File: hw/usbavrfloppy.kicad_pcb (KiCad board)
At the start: 2 copper layers, 96.5 x 70.5 mm, 65 parts, among them CON1 CONN_02X03, J1 bothdrv, J2 floppy_conn, J3 floppy_power, J5 USB_B, J6 PWRIN, J7 USB_OTG, P1 CONN_01X03, P2 CONN_01X01, P3 CONN_01X01, P4 CONN_01X01, P5 CONN_01X01, Q1 BSS138, Q10 BSS138, Q2 BSS138, Q3 BSS138, Q4 BSS138, Q5 BSS138, Q6 BSS138, Q7 BSS138, Q8 BSS138, Q9 BSS138, SW1 ~mRESET, U1 ATMEGA88-A, U2 FT232RL, Y1 16MHz

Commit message: First Kicad 5 import
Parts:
- removed G***: LOGO, RetroBitLab:amigaLogo_BW_31x12mm
- removed OSHW: Symbol_OSHW-Logo_SilkScreen, Symbols:Symbol_OSHW-Logo_SilkScreen
- removed WB: LOGO, RetroBitLab:amigaWorkBench1-SIlkScreenBack
- added AmigaLogo: LOGO, RetroBitLab:amigaLogo_BW_31x12mm, B.Cu at (151.8, 105.4)
- added J4: FPC Floppy, RetroBitLab:HLW26R-6C7LF, B.Cu at (152.4, 125.7)
- added KicadLogo: KiCad-Logo2_5mm_SilkScreen, Symbol:KiCad-Logo2_5mm_SilkScreen, F.Cu at (158.8, 88.3)
- added WBLogo: LOGO, RetroBitLab:amigaWorkBench1, B.Cu at (184.2, 69.8)
- C1, C2, C3, C4, C6: footprint Capacitors_SMD:C_1206_HandSoldering -> Capacitor_SMD:C_1206_3216Metric_Pad1.33x1.80mm_HandSolder
- C5: footprint Capacitors_SMD:c_elec_5x5.7 -> Capacitor_Tantalum_SMD:CP_EIA-3216-18_Kemet-A_Pad1.58x1.35mm_HandSolder
- CON1: value CONN_02X03 -> Conn_02x03; footprint Pin_Headers:Pin_Header_Angled_2x03 -> Connector_PinHeader_2.54mm:PinHeader_2x03_P2.54mm_Horizontal
- D1, D2, D3: footprint LEDs:LED_1206 -> LED_SMD:LED_1206_3216Metric_Pad1.42x1.75mm_HandSolder
- J1: footprint Pin_Headers:Pin_Header_Straight_1x02 -> Connector_PinHeader_2.54mm:PinHeader_1x02_P2.54mm_Vertical
- J3: footprint Pin_Headers:Pin_Header_Straight_1x04 -> Connector_PinHeader_2.54mm:PinHeader_1x04_P2.54mm_Vertical
- J6: footprint Pin_Headers:Pin_Header_Angled_1x04 -> Connector_PinHeader_2.54mm:PinHeader_1x04_P2.54mm_Horizontal
- P1: footprint Pin_Headers:Pin_Header_Straight_1x03 -> Connector_PinHeader_2.54mm:PinHeader_1x03_P2.54mm_Vertical
- P2, P3, P4, P5: footprint Connect:1pin -> MountingHole:MountingHole_3mm
- Q1, Q10, Q2, Q3, Q4, Q5, Q6, Q7, Q8, Q9: footprint TO_SOT_Packages_SMD:SOT-23 -> Package_TO_SOT_SMD:SOT-23
- R1, R10, R11, R12, R13, R14, R15, R16, R17, R18, R19, R2, R20, R21, R22, R23, R24, R25, R26, R27, R3, R4, R5, R6, R7, R8, R9: footprint Resistors_SMD:R_1206_HandSoldering -> Resistor_SMD:R_1206_3216Metric_Pad1.30x1.75mm_HandSolder
- U1: value ATMEGA88-A -> ATmega88PA-AU; footprint Housings_QFP:TQFP-32_7x7mm_Pitch0.8mm -> Package_QFP:TQFP-32_7x7mm_P0.8mm
- U2: footprint Housings_SSOP:SSOP-28_5.3x10.2mm_Pitch0.65mm -> Package_SO:SSOP-28_5.3x10.2mm_P0.65mm
- Y1: footprint Crystals:Crystal_HC49-SD_SMD -> Crystal:Crystal_HC49-4H_Vertical
- moved P4 15.2 mm to (196.8, 62.2)
- moved J6 11.7 mm to (177.8, 68.6)
- moved C4 2.83 mm to (126.0, 88.9)
- moved Y1 2.54 mm to (147.3, 80.0)
- moved C5 1.27 mm to (128.3, 82.5), turned to 270 degrees
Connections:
- J2 pad 2: (no net) -> Net-(J2-Pad2)
- J2 pad 34: (no net) -> Net-(J2-Pad34)
- J2 pad 4: (no net) -> Net-(J2-Pad4)
- J2 pad 6: (no net) -> Net-(J2-Pad6)
- J7 pad 4: (no net) -> Net-(J7-Pad4)
- P2 pad 1: (no net) -> Net-(P2-Pad1)
- P3 pad 1: (no net) -> Net-(P3-Pad1)
- P4 pad 1: (no net) -> Net-(P4-Pad1)
- P5 pad 1: (no net) -> Net-(P5-Pad1)
- U1 pad 14: (no net) -> Net-(U1-Pad14)
- U1 pad 19: (no net) -> Net-(U1-Pad19)
- U1 pad 20: (no net) -> Net-(U1-Pad20)
- U1 pad 22: (no net) -> Net-(U1-Pad22)
- U1 pad 26: (no net) -> Net-(U1-Pad26)
- U1 pad 27: (no net) -> Net-(U1-Pad27)
- U1 pad 28: (no net) -> Net-(U1-Pad28)
- U2 pad 10: (no net) -> Net-(U2-Pad10)
- U2 pad 12: (no net) -> Net-(U2-Pad12)
- U2 pad 13: (no net) -> Net-(U2-Pad13)
- U2 pad 14: (no net) -> Net-(U2-Pad14)
- U2 pad 19: (no net) -> Net-(U2-Pad19)
- U2 pad 2: (no net) -> Net-(U2-Pad2)
- U2 pad 22: (no net) -> Net-(U2-Pad22)
- U2 pad 23: (no net) -> Net-(U2-Pad23)
- U2 pad 27: (no net) -> Net-(U2-Pad27)
- U2 pad 28: (no net) -> Net-(U2-Pad28)
- U2 pad 3: (no net) -> Net-(U2-Pad3)
- U2 pad 6: (no net) -> Net-(U2-Pad6)
- U2 pad 9: (no net) -> Net-(U2-Pad9)
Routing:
- net Vcc_FLOPPY: track 318.4 -> 361.1 mm, vias 2 -> 1
- net GND: track 316.1 -> 292.6 mm, vias 1 -> 0
- net /~WDATA: track 42.0 -> 60.2 mm
- net /~mMOTEN: track 51.3 -> 34.6 mm
- net /CTS: track 46.2 -> 29.7 mm, vias 0 -> 2
- net /~DIR: track 36.1 -> 51.2 mm, vias 1 -> 0
- net /~MOTEB: track 46.1 -> 59.8 mm, vias 1 -> 0
- net /~mRESET: track 64.1 -> 51.6 mm, vias 0 -> 2
- net /~STEP: track 39.9 -> 51.4 mm, vias 1 -> 0
- net /~SIDE1: track 51.9 -> 62.6 mm
- net /~RDATA: track 26.8 -> 37.2 mm, vias 1 -> 0
- net /~WGATE: track 30.4 -> 40.4 mm
- net /~WPROT: track 23.3 -> 33.1 mm, vias 1 -> 0
- net VCC_USB: track 30.0 -> 37.1 mm, vias 2 -> 1
- net +12V: track 40.3 -> 34.8 mm
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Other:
- board text added: "Original concept on GitHub: RobSmithDev/ArduinoFloppyDiskReader"
- board text added: "P1 (1-2) = External VCC P1 (2-3) = USB Powered (max 500mA)"
- board text added: "RBL003.6"
- board text added: "designed by R.G. 2018/2019/2021"
- board text added: "https://github.com/gianlucarenzi/waffle-usbamigafloppy"
- board text removed: "RBL003.5"
- board text removed: "RETROBIT LAB"
- board text removed: "designed by R.G. 2018/2019"

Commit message: Updated
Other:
- board text added: "pin 1"
- board text added: "pin 26"

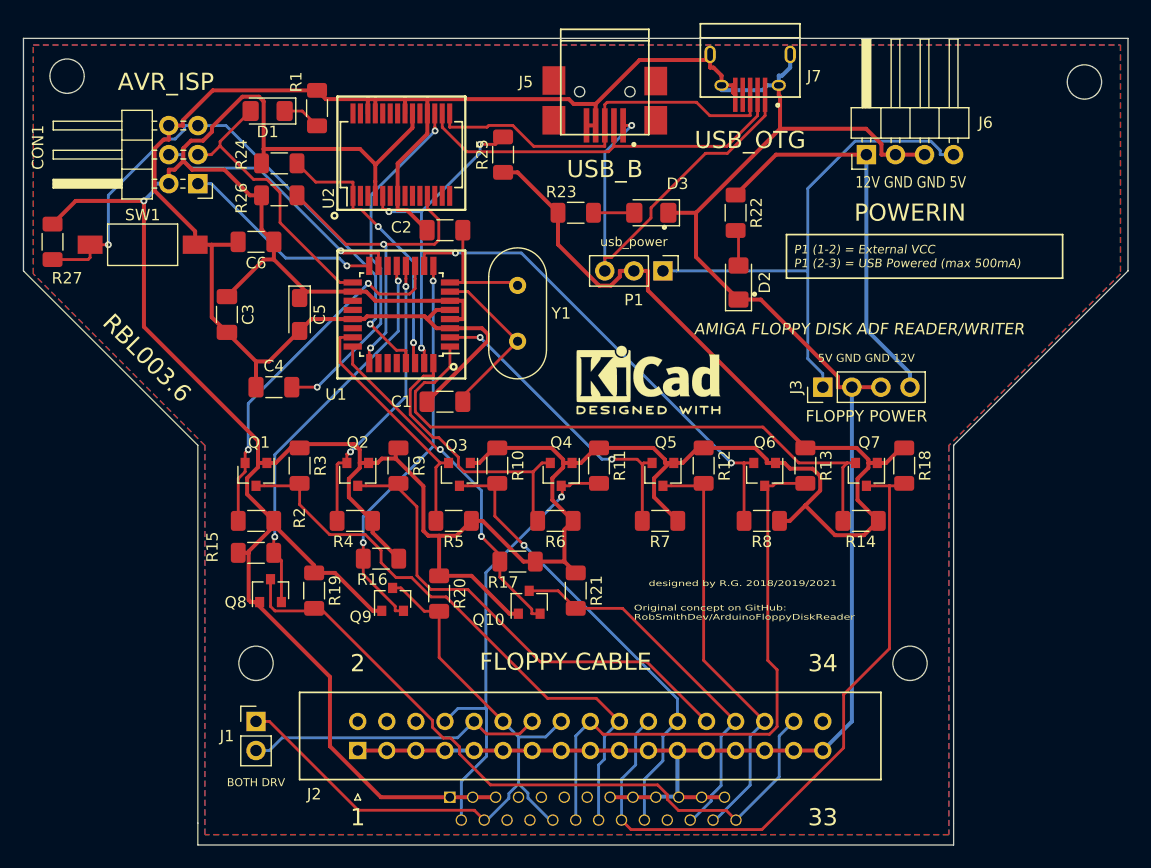
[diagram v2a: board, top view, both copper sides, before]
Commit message: Modified for final Kicad 5
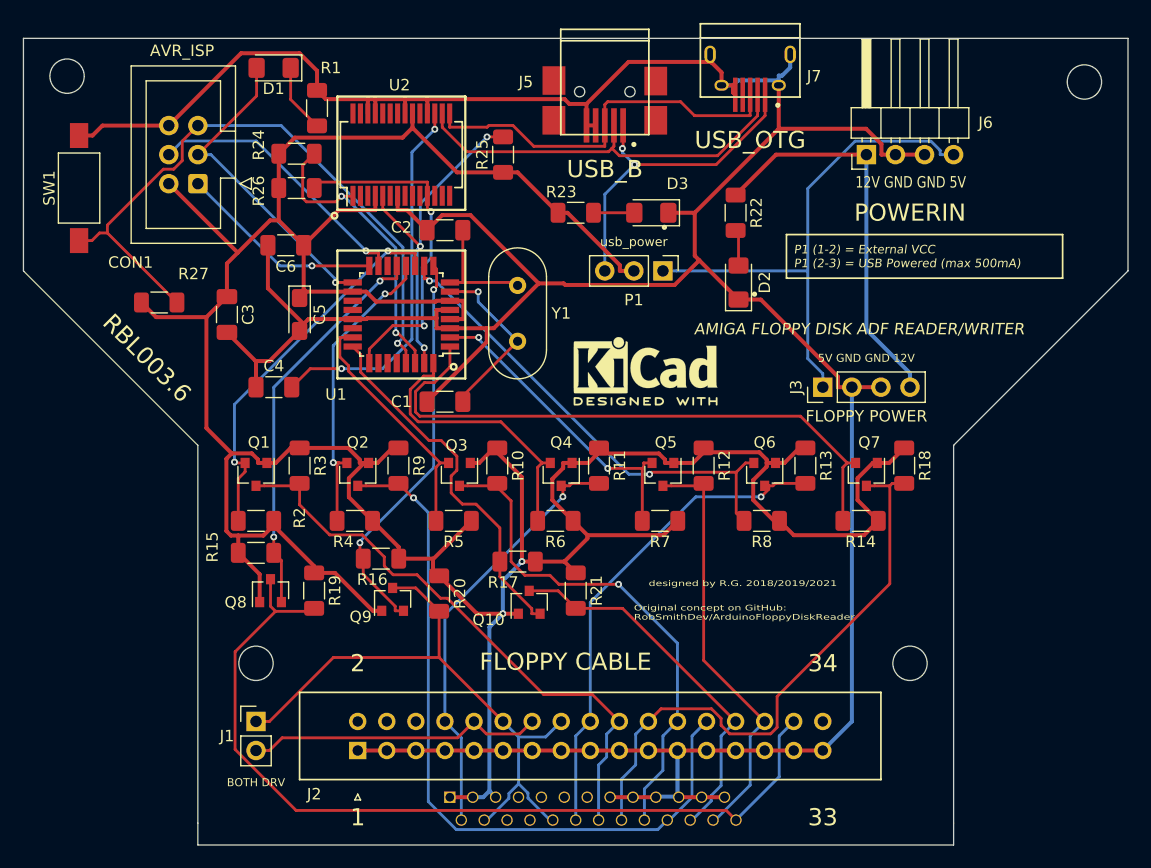
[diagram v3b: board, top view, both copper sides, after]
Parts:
- removed AmigaLogo: LOGO, RetroBitLab:amigaLogo_BW_31x12mm
- removed KicadLogo: KiCad-Logo2_5mm_SilkScreen, Symbol:KiCad-Logo2_5mm_SilkScreen
- removed WBLogo: LOGO, RetroBitLab:amigaWorkBench1
- added AMIGALOGO: LOGO, RetroBitLab:amigaLogo_BW_31x12mm, B.Cu at (152.8, 105.0)
- added LOGO: KiCad-Logo2_5mm_SilkScreen, Symbol:KiCad-Logo2_5mm_SilkScreen, F.Cu at (158.5, 87.5)
- added WBLOGO: LOGO, RetroBitLab:amigaWorkBench1, B.Cu at (183.2, 73.5)
- CON1: footprint Connector_PinHeader_2.54mm:PinHeader_2x03_P2.54mm_Horizontal -> Connector_IDC:IDC-Header_2x03_P2.54mm_Vertical
- moved R27 10.7 mm to (116.0, 81.5), turned to 180 degrees
- moved SW1 7.44 mm to (109.0, 71.5), turned to 90 degrees
- moved D1 3.81 mm to (126.0, 61.0)
- moved C6 2.62 mm to (127.1, 76.5)
- moved R24 1.73 mm to (128.0, 68.5)
- moved R26 1.64 mm to (128.0, 71.5)
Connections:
- J4 pad 20: Net-(J4-Pad20) -> /~TRK0
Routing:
- net Vcc_FLOPPY: track 361.1 -> 308.7 mm, vias 1 -> 2
- net /~TRK0: track 42.8 -> 65.0 mm, vias 0 -> 1
- net GND: track 292.6 -> 313.1 mm
- net /~SIDE1: track 62.6 -> 77.0 mm
- net /~WDATA: track 60.2 -> 51.4 mm
- net /~DIR: track 51.2 -> 43.2 mm, vias 0 -> 1
- net VCC_USB: track 37.1 -> 29.3 mm, vias 1 -> 2
- net /~mRESET: track 51.6 -> 57.6 mm, vias 2 -> 1
- net /~MOTEB: track 59.8 -> 54.6 mm
- net /~WGATE: track 40.4 -> 44.8 mm
- net /SCK: track 24.5 -> 28.0 mm, vias 0 -> 1
- net /~INDEX: track 40.3 -> 37.6 mm
- net Net-(D1-Pad1): track 3.37 -> 6.02 mm
- net /RXD: track 24.1 -> 26.5 mm
- net /~mSTEP: track 32.1 -> 33.8 mm
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- removed copper zone on B.Cu, net GND
- removed copper zone on F.Cu, net GND

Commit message: Sent to JLCPCB 5th April 2021
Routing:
- added copper zone on B.Cu, net GND
- added copper zone on F.Cu, net GND
